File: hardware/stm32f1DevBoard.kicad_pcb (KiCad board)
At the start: 2 copper layers, 100 x 50 mm, 67 parts, among them J1 USB_2, J2 POWER_JACK, J3 SDCARD, M1 Mounting Hole, M2 Mounting Hole, M3 Mounting Hole, M4 Mounting Hole, P1 JTAG, P2 P20, P3 P20, P4 WIFIDEBUG, Q1 MOSFET-P, U1 STM32F102C6, U2 MRF24WB0MX, U3 LM358, U4 VREG-X-5, U5 VREG-5-3.3, X1 32,768Hz, X2 20MHz

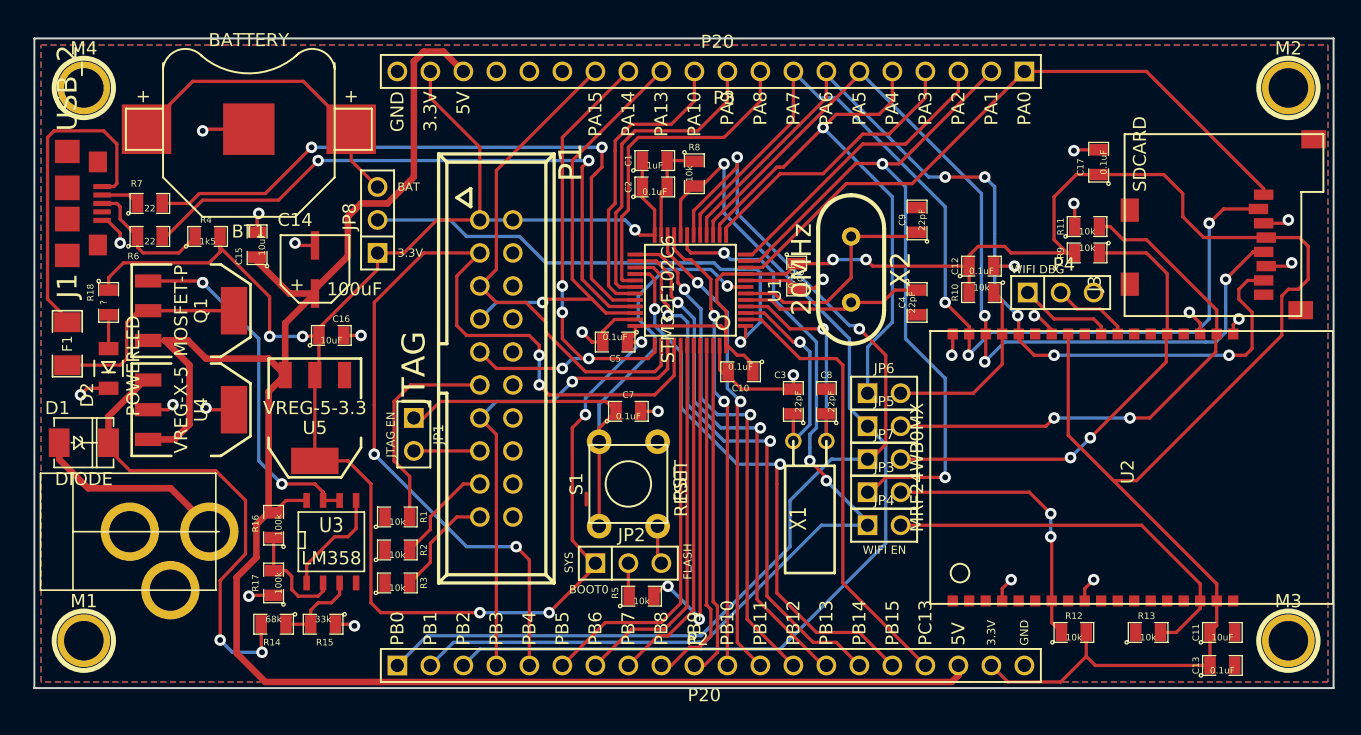
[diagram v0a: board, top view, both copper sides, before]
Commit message: fix sdcard
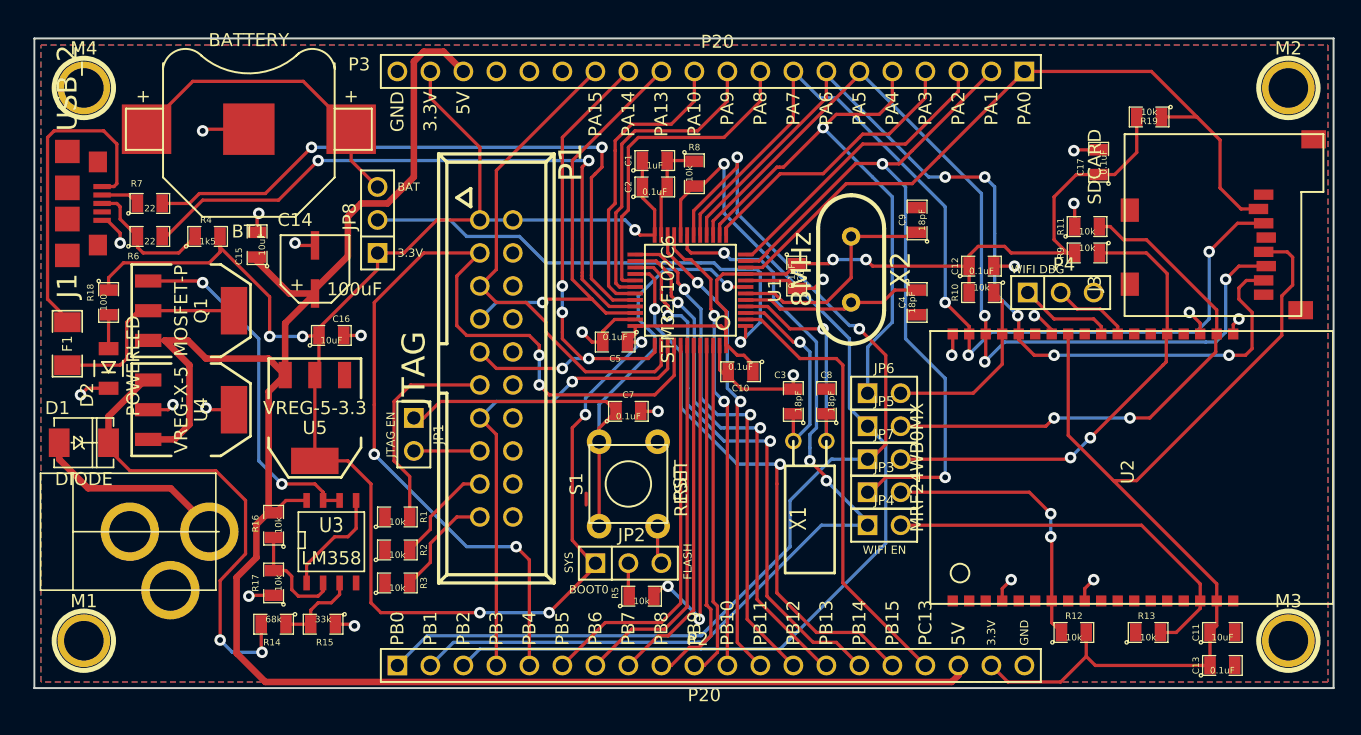
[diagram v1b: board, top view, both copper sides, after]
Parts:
- added R19: 10k, SM0805, F.Cu at (185.8, 106.0)
- C3, C4, C8, C9: value 22pF -> 18pF
- R16, R17: value 100k -> 10k
- R18: value ? -> 100
- X2: value 20MHz -> 8MHz
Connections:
- J3 pad 1: SDCS -> (no net)
- J3 pad 2: MOSI -> SDCS
- J3 pad 3: GND -> MOSI
- J3 pad 4: +3.3V -> GND
- J3 pad 5: SCK -> +3.3V
- J3 pad 6: GND -> SCK
- J3 pad 9: (no net) -> GND
- P3 pad 15: (no net) -> GND
- P3 pad 16: (no net) -> GND
- P3 pad 17: (no net) -> GND
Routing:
- net +3.3V: track 294.6 -> 282.1 mm
- net SDCS: track 50.3 -> 55.0 mm
- net GND: track 75.4 -> 71.4 mm, vias 25 -> 23
- net MOSI: track 75.1 -> 73.8 mm

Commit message: fixed sdcard
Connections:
- J3 pad 4: GND -> +3.3V
- J3 pad 5: +3.3V -> SCK
- J3 pad 6: SCK -> GND
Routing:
- net SCK: track 70.8 -> 72.0 mm
- net +3.3V: track 282.1 -> 282.9 mm
- net MOSI: track 73.8 -> 74.4 mm

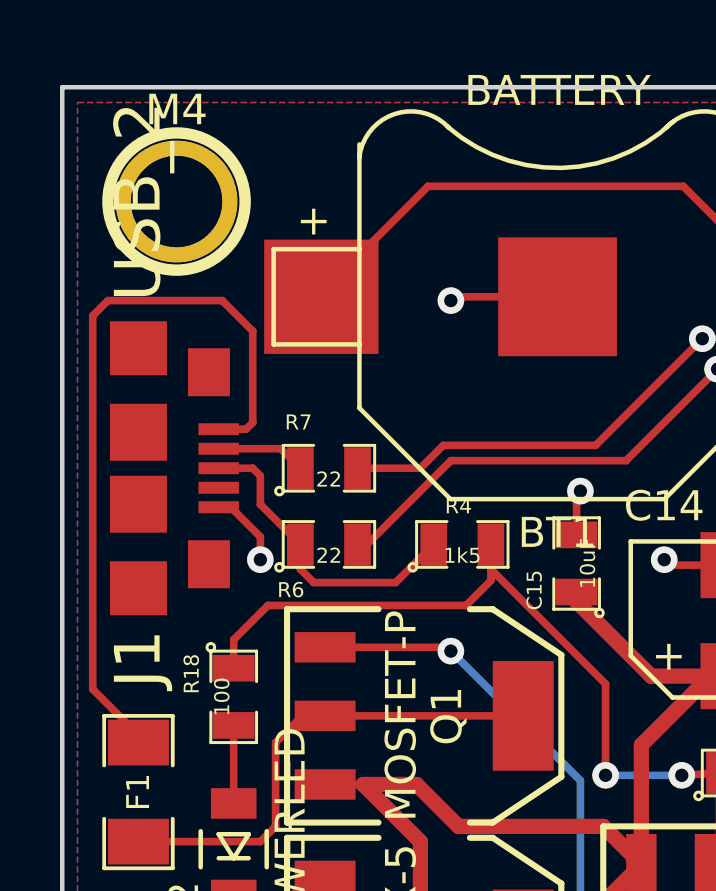
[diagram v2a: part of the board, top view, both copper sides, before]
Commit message: usb renumber
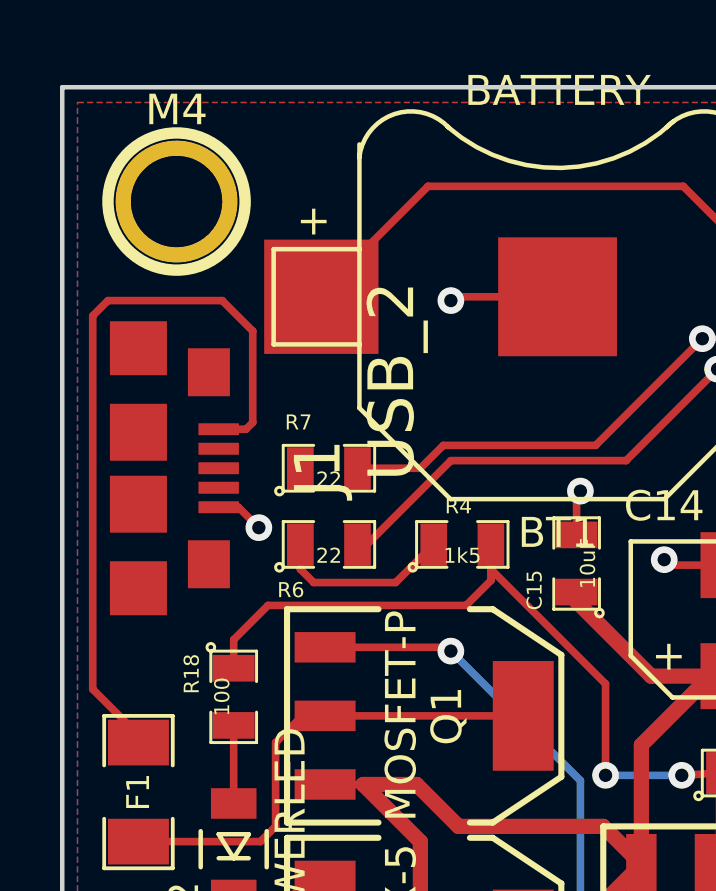
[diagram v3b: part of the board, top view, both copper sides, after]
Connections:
- J1 pad 2: N-0000012 (its old number) -> /USBD-
- J1 pad 3: N-0000013 (its old number) -> /USBD+
- J1 pad 4: GND -> (no net)
- J1 pad 5: (no net) -> GND
- R4 pad 1: N-0000012 (its old number) -> /USBD+
- R6 pad 1: N-0000012 (its old number) -> /USBD+
- R7 pad 1: N-0000013 (its old number) -> /USBD-
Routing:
- net N-0000012 (its old number): track 10.3 -> 0.00 mm
- net /USBD+: track 0.00 -> 5.98 mm
- net N-0000013 (its old number): track 2.99 -> 0.00 mm
- net GND: track 71.4 -> 70.4 mm

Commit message: update hardware
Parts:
- removed JP1: JTAG_ENABLE, PIN_ARRAY_2X1
- added C18: 100uF, CAP-CAN-5mm, F.Cu at (123.2, 123.1)
- added C19: 47pF, SM0805, F.Cu at (113.0, 114.8)
- added C20: 47pF, SM0805, F.Cu at (109.0, 110.5)
- added D3: DIODESCH, DO-214AC(SMA), F.Cu at (103.9, 126.4)
- added Q2: MOSFET-P, SOT23, F.Cu at (106.4, 120.3)
- added R20: 10k, SM0805, F.Cu at (113.0, 117.0)
- D1: value DIODE -> DIODESCH
- moved R3 22.5 mm to (128.8, 119.4)
- moved R2 17.7 mm to (128.8, 121.7)
- moved R1 12.9 mm to (128.8, 124.0)
- moved JP8 11.4 mm to (135.6, 107.3), turned to 180 degrees
- moved C16 6.75 mm to (128.8, 126.1)
- moved R18 4.86 mm to (108.5, 124.3)
- moved U5 4.73 mm to (125.3, 132.1), turned to 270 degrees
- moved R4 4.70 mm to (109.0, 117.0), turned to 180 degrees
- moved D2 4.25 mm to (108.5, 128.7)
- moved R17 2.90 mm to (119.2, 144.7)
- moved R14 2.90 mm to (119.2, 147.9)
- moved R15 2.90 mm to (123.0, 147.9)
- moved R16 2.90 mm to (119.2, 140.3)
- moved U3 2.90 mm to (123.6, 141.5)
- moved U4 2.87 mm to (114.8, 129.4)
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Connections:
- net N-0000015 renamed USBDISC
- F1 pad 2: VUSB -> N-0000020
- P1 pad 15: N-000007 (its old number) -> nRST
- R4 pad 1: /USBD+ -> N-0000053
- R4 pad 2: +3.3V -> N-0000023
- R6 pad 2: N-000009 (its old number) -> N-0000053
- U1 pad 33: N-000009 (its old number) -> N-0000053
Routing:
- net USBDISC: track 26.0 -> 118.8 mm, vias 0 -> 1
- net N-000009 (its old number): track 49.5 -> 0.00 mm, vias 2 -> 0
- net N-0000053: track 0.00 -> 47.2 mm, vias 0 -> 2
- net nJTRST: track 74.8 -> 34.8 mm, vias 4 -> 0
- net +3.3V: track 282.9 -> 304.9 mm, vias 9 -> 6
- net JTDI: track 39.1 -> 56.4 mm, vias 0 -> 3
- net GND: track 70.4 -> 56.9 mm, vias 23 -> 16
- net +5V: track 146.4 -> 137.4 mm, vias 0 -> 4
- net VBAT: track 38.5 -> 30.0 mm
- net N-0000038: track 16.5 -> 8.12 mm
- net JTDO: track 37.4 -> 42.9 mm, vias 1 -> 0
- net N-000007 (its old number): track 5.08 -> 0.00 mm
- net nRST: track 49.0 -> 53.4 mm
- net N-0000080: track 27.6 -> 31.6 mm
- net JTCK: track 40.4 -> 36.4 mm, vias 4 -> 3
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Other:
- board text removed: "JTAG EN"
